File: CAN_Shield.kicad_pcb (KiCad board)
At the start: 2 copper layers, 65 x 56.5 mm, 28 parts, among them J1 GPIO, U1 ATECC608A-SSHDA-T, U2 MCP2515T-I/SO, U4 SN65HVD230DR, X1 X322516MLB4SI, j2 DB128V-5.08-5P-GN-S, j3 DB128V-5.08-7P-GN-S, j4 DB128V-5.08-7P-GN-S

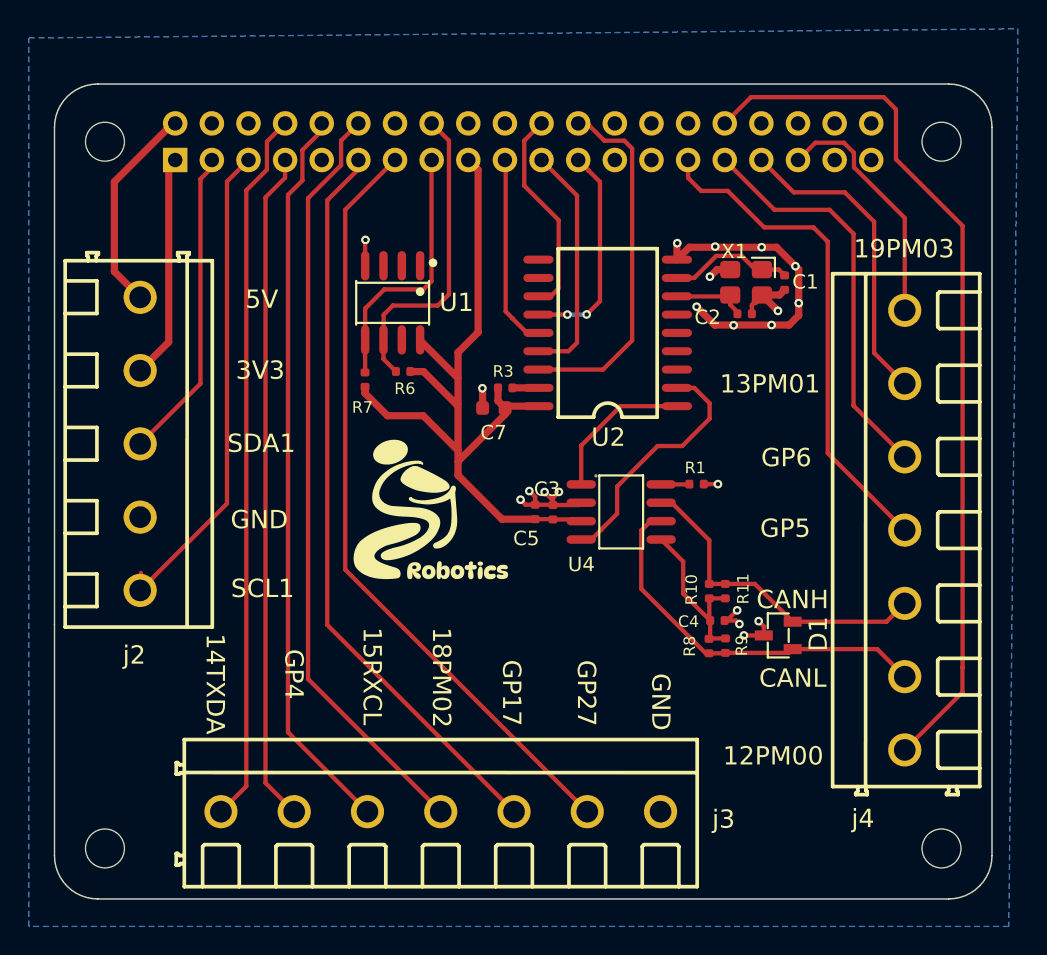
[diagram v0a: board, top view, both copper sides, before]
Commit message: Quick fix from EzSeperateI2C
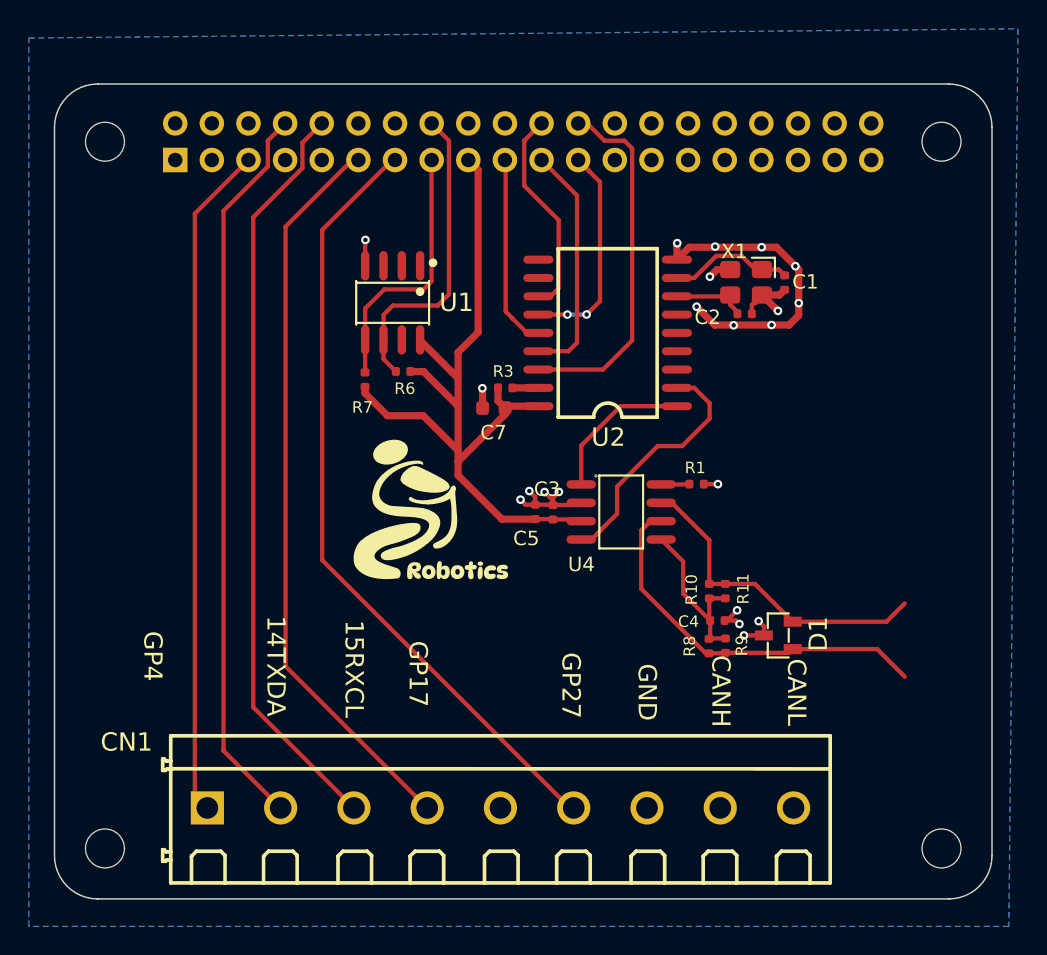
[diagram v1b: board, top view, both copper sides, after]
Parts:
- removed j2: DB128V-5.08-5P-GN-S, ImportFP:CONN-TH_5P-P5.08_DIBO_DB128V-5.08-5P-GN-S
- removed j3, j4: DB128V-5.08-7P-GN-S, ImportFP:CONN-TH_7P-P5.08_DIBO_DB128V-5.08-7P-GN-S
- added CN1: DB128V-5.08-9P-GN-S, ImportFP:CONN-TH_9P-P5.08_DIBO_DB128V-5.08-9P-GN-S, F.Cu at (130.9, 93.7)
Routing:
- net /GPIO12/PWM0: track 61.0 -> 0.00 mm
- net /GPIO18/PCM.CLK: track 53.0 -> 0.00 mm
- net /GPIO4/GPCLK0: track 46.6 -> 0.00 mm
- net /GPIO5: track 35.0 -> 0.00 mm
- net /GPIO6: track 28.0 -> 0.00 mm
- net /GPIO2/SDA1: track 21.7 -> 0.00 mm
- net /GPIO13/PWM1: track 21.7 -> 0.00 mm
- net /GPIO19/PCM.FS: track 17.7 -> 0.65 mm
- net +3V3: track 73.7 -> 58.1 mm
- net +5V: track 14.6 -> 0.00 mm
- net /GPIO3/SCL1: track 34.8 -> 47.6 mm
- net /GPIO15/RXD0: track 51.0 -> 52.5 mm
- net /GPIO14/TXD0: track 49.6 -> 50.9 mm
- net /GPIO27: track 53.6 -> 54.4 mm
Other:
- board text removed: "12PM00"
- board text removed: "13PM01"
- board text removed: "18PM02"
- board text removed: "19PM03"
- board text removed: "3V3"
- board text removed: "5V"
- board text removed: "GP5"
- board text removed: "GP6"
- board text removed: "SCL1"
- board text removed: "SDA1"

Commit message: Finished DesktopShield layout but still not gen production file
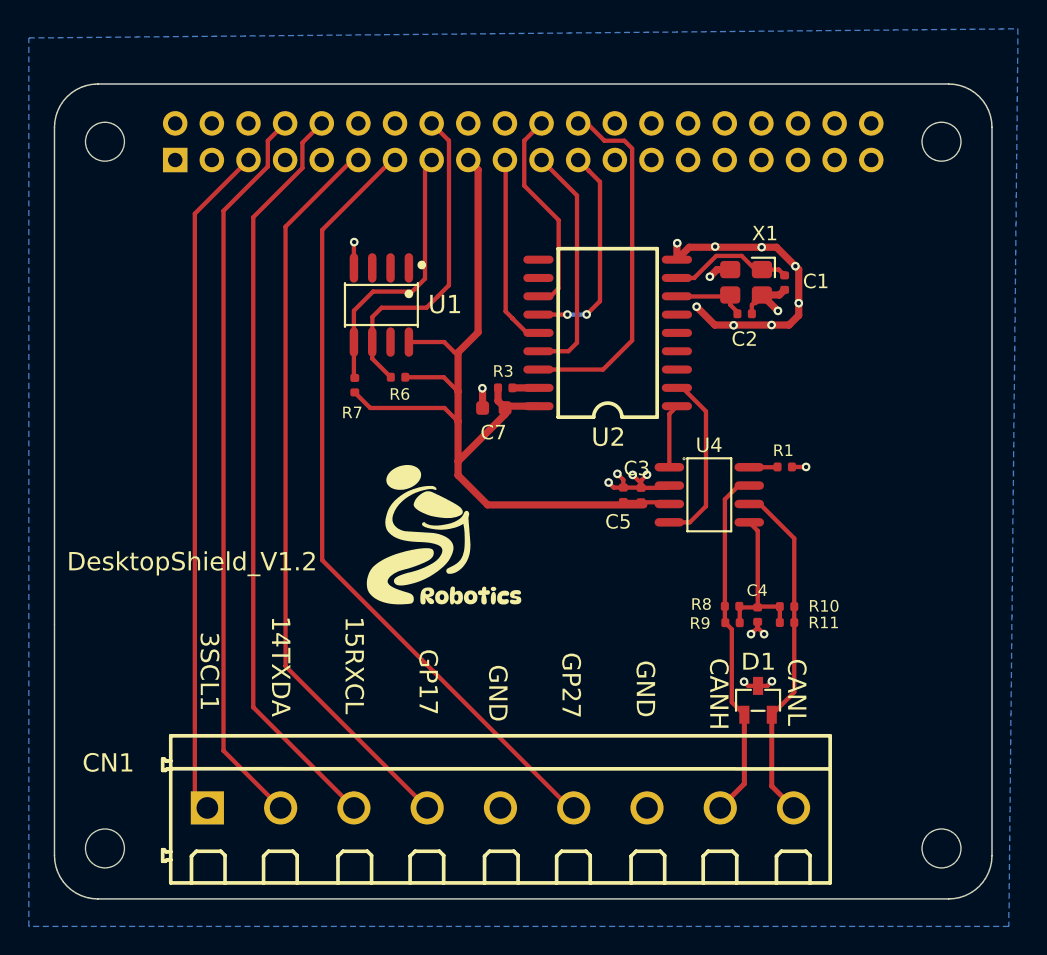
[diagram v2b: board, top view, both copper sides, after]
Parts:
- moved U4 6.22 mm to (145.4, 72.0)
- moved C3 6.22 mm to (140.7, 72.0)
- moved C5 6.22 mm to (139.4, 72.0)
- moved R1 6.22 mm to (150.6, 70.0)
- moved R10 5.50 mm to (150.8, 79.7), turned to 180 degrees
- moved R11 4.80 mm to (150.8, 80.8), turned to 180 degrees
- moved D1 4.71 mm to (148.8, 86.2), turned to 0 degrees
- moved R8 3.19 mm to (147.0, 79.7), turned to 0 degrees
- moved C4 2.82 mm to (148.8, 80.3), turned to -90 degrees
- moved G*** 1.98 mm to (127.0, 74.8)
- moved R9 1.66 mm to (147.0, 80.8), turned to 0 degrees
- moved R7 0.81 mm to (120.8, 64.4)
- moved U1 0.79 mm to (122.7, 58.8)
- moved R6 0.53 mm to (123.8, 63.8)
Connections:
- D1 pad 1: /CAN_D- -> /CAN_D+
- D1 pad 2: /CAN_D+ -> /CAN_D-
- R10 pad 1: /CAN_D+ -> /CAN_D-
- R11 pad 1: /CAN_D+ -> /CAN_D-
- R8 pad 1: /CAN_D- -> /CAN_D+
- R9 pad 1: /CAN_D- -> /CAN_D+
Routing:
- net +3V3: track 58.1 -> 64.6 mm
- net /TXCAN: track 11.1 -> 5.10 mm
- net /RXCAN: track 18.0 -> 13.0 mm
- net /CAN_D-: track 26.7 -> 24.1 mm
- net /CAN_D+: track 22.6 -> 24.7 mm
- net /GPIO23: track 21.1 -> 22.0 mm
- net Net-(U4-VREF): track 12.2 -> 11.3 mm
- net GND: track 45.9 -> 45.1 mm
- net /GPIO22: track 18.8 -> 19.6 mm
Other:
- board text added: "3SCL1"
- board text added: "DesktopShield_V1.2"
- board text removed: "GP4"
